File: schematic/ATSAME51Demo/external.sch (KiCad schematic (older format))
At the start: 29 parts, among them IC3 MCP2221-I_SL, J10 Conn_02x06_Odd_Even, J11 Conn_02x07_Odd_Even, J12 Conn_01x02, J13 Conn_01x08, J14 Conn_02x08_Odd_Even, J15 Conn_02x06_Odd_Even, J16 Conn_02x07_Odd_Even, J7 Conn_02x02_Odd_Even, J8 Conn_02x02_Odd_Even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

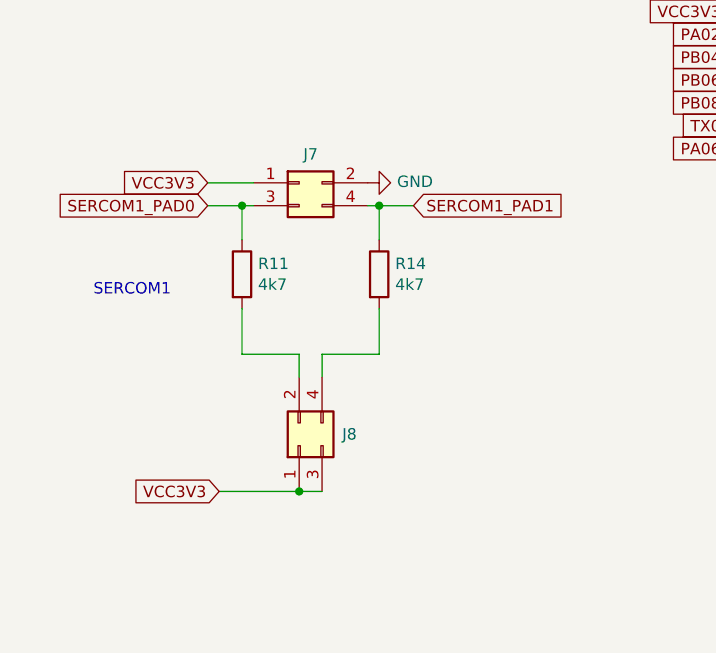
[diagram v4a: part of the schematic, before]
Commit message: Added  USB_VBUS_SENSE
And other minor improvements
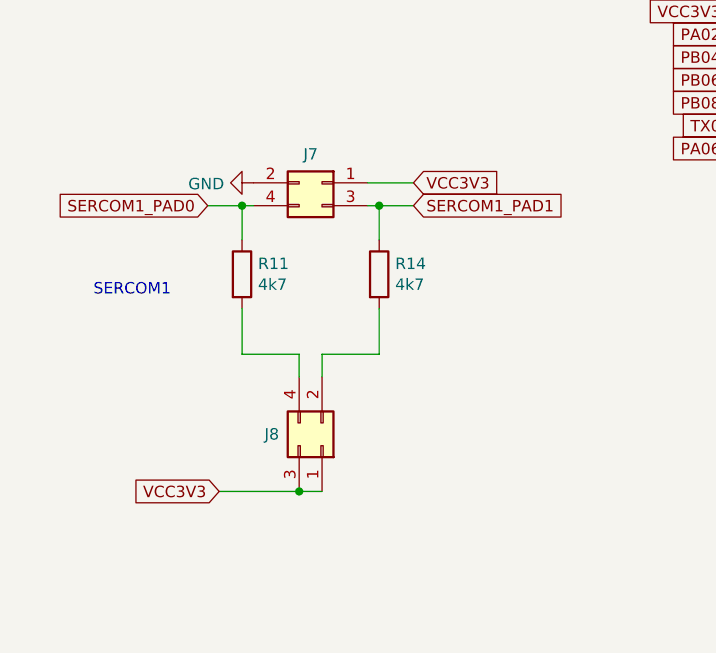
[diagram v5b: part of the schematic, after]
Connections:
- net SERCOM1_PAD0: now also J7.4 (Pin_4); no longer J7.3 (Pin_3)
- net SERCOM1_PAD1: now also J7.3 (Pin_3); no longer J7.4 (Pin_4)
- net at J8.2 (Pin_2): now also R14.2; no longer R11.2
- net at J8.4 (Pin_4): now also R11.2; no longer R14.2
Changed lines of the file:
@@
 L Connector_Generic:Conn_02x02_Odd_Even J7
 U 1 1 6175F2EC
-P 1900 5750
-F 0 "J7" H 1950 5875 50  0000 C CNN
-F 1 "Conn_02x02_Odd_Even" H 1950 5876 50  0001 C CNN
-F 2 "Connector_PinHeader_2.54mm:PinHeader_2x02_P2.54mm_Vertical" H 1900 5750 50  0001 C CNN
-F 3 "~" H 1900 5750 50  0001 C CNN
-	1    1900 5750
-	1    0    0    -1
+P 2000 5750
+F 0 "J7" H 2050 5875 50  0000 C CNN
+F 1 "Conn_02x02_Odd_Even" H 2050 5876 50  0001 C CNN
+F 2 "Connector_PinHeader_2.54mm:PinHeader_2x02_P2.54mm_Vertical" H 2000 5750 50  0001 C CNN
+F 3 "~" H 2000 5750 50  0001 C CNN
+	1    2000 5750
+	-1   0    0    -1
 $EndComp
 $Comp
 L Connector_Generic:Conn_02x02_Odd_Even J8
 U 1 1 6175FDD7
-P 1900 6900
-F 0 "J8" V 1950 6712 50  0000 R CNN
-F 1 "Conn_02x02_Odd_Even" H 1950 7026 50  0001 C CNN
-F 2 "Connector_PinHeader_2.54mm:PinHeader_2x02_P2.54mm_Vertical" H 1900 6900 50  0001 C CNN
-F 3 "~" H 1900 6900 50  0001 C CNN
-	1    1900 6900
-	0    -1   -1   0
+P 2000 6900
+F 0 "J8" V 2050 6712 50  0000 R CNN
+F 1 "Conn_02x02_Odd_Even" H 2050 7026 50  0001 C CNN
+F 2 "Connector_PinHeader_2.54mm:PinHeader_2x02_P2.54mm_Vertical" H 2000 6900 50  0001 C CNN
+F 3 "~" H 2000 6900 50  0001 C CNN
+	1    2000 6900
+	0    1    -1   0
 $EndComp
 Text GLabel 1550 7100 0    50   Input ~ 0
@@
 Wire Wire Line
 	2400 4500 2600 4500
-Text GLabel 1500 5750 0    50   Input ~ 0
+Text GLabel 2400 5750 2    50   Input ~ 0
 VCC3V3
 $Comp
 L power:GND #PWR028
 U 1 1 6181EDC9
-P 2200 5750
-F 0 "#PWR028" H 2200 5500 50  0001 C CNN
-F 1 "GND" V 2205 5622 50  0000 R CNN
-F 2 "" H 2200 5750 50  0001 C CNN
-F 3 "" H 2200 5750 50  0001 C CNN
-	1    2200 5750
-	0    -1   -1   0
+P 1700 5750
+F 0 "#PWR028" H 1700 5500 50  0001 C CNN
+F 1 "GND" V 1705 5622 50  0000 R CNN
+F 2 "" H 1700 5750 50  0001 C CNN
+F 3 "" H 1700 5750 50  0001 C CNN
+	1    1700 5750
+	0    1    1    0
 $EndComp
 Text GLabel 1500 5850 0    50   Input ~ 0
@@
 SERCOM1_PAD1
 Wire Wire Line
-	1500 5750 1700 5750
-Wire Wire Line
 	2200 5850 2250 5850
-Wire Wire Line
-	1500 5850 1650 5850
 Wire Wire Line
 	1650 6000 1650 5850
@@
 Wire Wire Line
 	2000 7100 1900 7100
-Wire Wire Line
-	1900 7100 1550 7100
-Connection ~ 1900 7100
 Text GLabel 3800 5000 0    50   Input ~ 0
 VCC3V3
@@
 Wire Wire Line
 	3000 3600 3000 3900
+Wire Wire Line
+	1500 5850 1650 5850
+Wire Wire Line
+	2200 5750 2400 5750
+Wire Wire Line
+	1550 7100 1900 7100
+Connection ~ 1900 7100
 $EndSCHEMATC
